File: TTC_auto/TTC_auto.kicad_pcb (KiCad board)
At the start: 2 copper layers, 84.2 x 84.2 mm, 78 parts, among them J1 EPS 3V3, J2 MISSION, J3 SMA edge, J4 SWD TC2030, J5 OBC I2C, J6 OBC UART, J7 EPS 5V, J8 SPARE GPIO, J9 DIPOLE FEED, Q1 AO3401A, U1 TPS7A2033PDBVR, U2 RFM98W-433S2, U3 STM32F446RET6, U4 TMP102, Y1 8MHz, Y2 32.768kHz

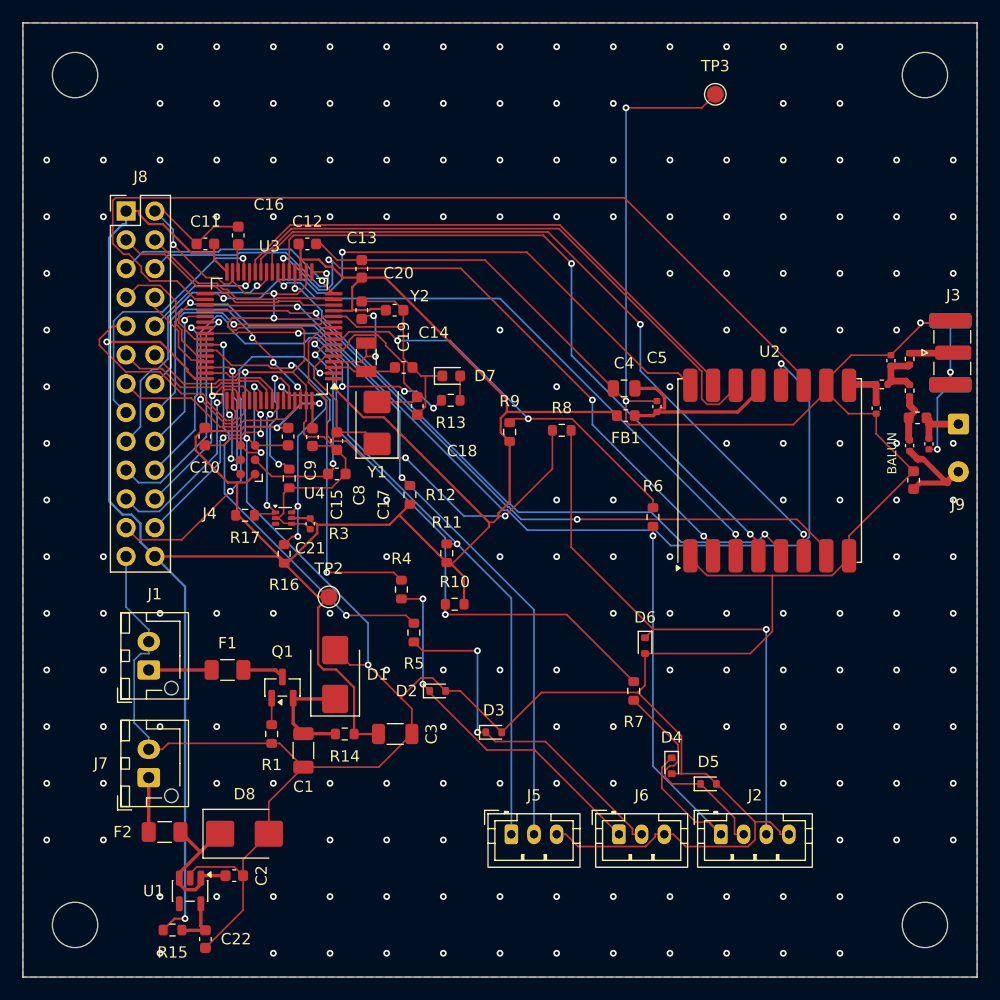
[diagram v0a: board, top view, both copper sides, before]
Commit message: TTC_auto: re-place by functional blocks (structured version)
Parts grouped into Power / MCU / RF / I/O / Sensor regions with
assembly spacing (~0.8 mm, 2 mm round MCU and RF module), crystal pads
matched to MCU pin order, copper keep-out under the RFM98W module,
3 fiducials, per-patch GND vias. Antenna/balun hand-fixed to top layer.
DRC: 0 violations, 0 unconnected, schematic parity clean.
README added.

Co-Authored-By: Claude Opus 5.5 <noreply@anthropic.com>
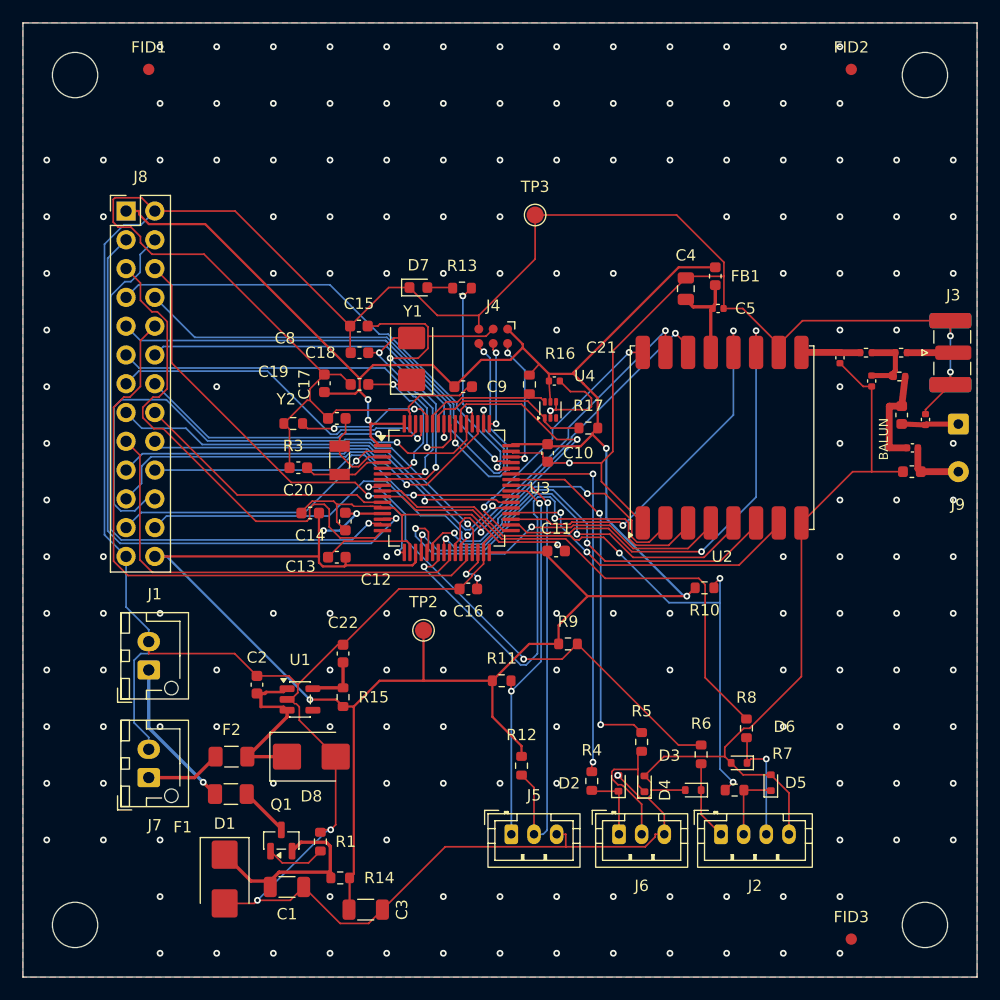
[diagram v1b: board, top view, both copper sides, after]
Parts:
- added FID1: Fiducial, Fiducial_1mm_Mask2mm, F.Cu at (104.0, 97.0)
- added FID2: Fiducial, Fiducial_1mm_Mask2mm, F.Cu at (166.0, 97.0)
- added FID3: Fiducial, Fiducial_1mm_Mask2mm, F.Cu at (166.0, 173.8)
- moved C11 41.1 mm to (139.9, 139.5), turned to 0 degrees
- moved C16 37.2 mm to (132.2, 142.8), turned to 180 degrees
- moved R17 31.3 mm to (142.8, 128.7), turned to 0 degrees
- moved R8 30.9 mm to (156.8, 155.2), turned to 90 degrees
- moved C10 30.3 mm to (139.2, 130.8)
- moved C22 28.0 mm to (121.2, 148.6), turned to 90 degrees
- moved C12 27.8 mm to (120.6, 140.1), turned to 180 degrees
- moved R16 26.3 mm to (137.6, 124.8), turned to -90 degrees
- moved R12 25.9 mm to (136.9, 158.4), turned to 90 degrees
- moved R15 25.5 mm to (121.2, 152.4), turned to -90 degrees
- moved U4 25.4 mm to (139.4, 127.0), turned to 90 degrees
- moved C21 25.0 mm to (139.8, 124.5), turned to 0 degrees
- moved J4 24.2 mm to (134.4, 120.5), turned to 180 degrees
- moved R4 23.8 mm to (143.1, 159.8)
- moved C13 22.3 mm to (121.3, 136.9), turned to -90 degrees
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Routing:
- net /RFM_DIO4: track 80.7 -> 33.4 mm
- net /PB2: track 10.9 -> 55.5 mm, vias 1 -> 0
- net /PD2: track 17.1 -> 58.4 mm, vias 3 -> 1
- net /RFM_DIO3: track 82.6 -> 41.5 mm, vias 0 -> 2
- net Net-(D6-A1): track 49.7 -> 10.7 mm
- net /RFM_DIO5: track 64.3 -> 27.9 mm
- net /PA1: track 18.0 -> 52.5 mm, vias 0 -> 1
- net /PA0: track 20.8 -> 54.4 mm, vias 0 -> 1
- net Net-(D4-A1): track 39.7 -> 6.95 mm, vias 1 -> 0
- net /PC12: track 15.8 -> 48.2 mm
- net /PA11: track 11.7 -> 42.8 mm, vias 0 -> 1
- net /OBC_SCL: track 70.8 -> 39.8 mm, vias 2 -> 1
- net /PA12: track 8.14 -> 38.2 mm, vias 0 -> 1
- net /RFM_RESET: track 64.7 -> 36.4 mm
- net /RFM_DIO2: track 51.9 -> 23.7 mm
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
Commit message: TTC_auto: spread placement for soldering and debugging
Re-placed with larger block areas (MCU and RF use the top strip),
bigger minimum gaps (~1.2 mm small parts, ~3 mm round MCU/radio/debug
pad) and a soft spacing penalty under 2.5 mm, then re-routed with
Freerouting. Median gap to nearest part 0.83 -> 2.03 mm; parts closer
than 1 mm 61 -> 5. Antenna path 36.3 mm, top layer, 0 vias.
DRC: 0 violations, 0 unconnected, schematic parity clean.

Co-Authored-By: Claude Opus 5.5 <noreply@anthropic.com>
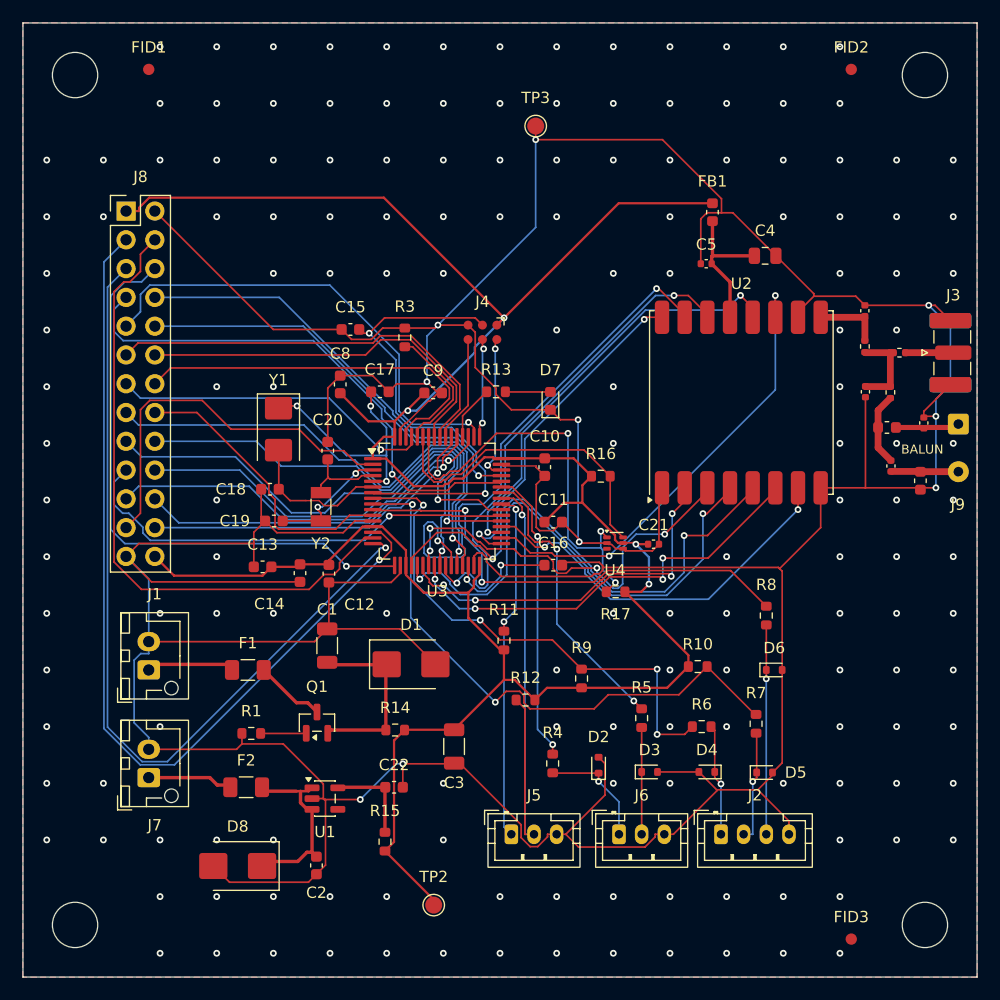
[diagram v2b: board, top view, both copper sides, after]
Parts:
- moved D1 25.1 mm to (127.2, 149.5), turned to 0 degrees
- moved TP2 24.3 mm to (129.2, 170.8), turned to 180 degrees
- moved C1 21.6 mm to (119.8, 147.8), turned to 90 degrees
- moved C21 16.9 mm to (148.6, 138.9)
- moved C2 16.8 mm to (118.8, 167.2), turned to -90 degrees
- moved C3 16.4 mm to (130.9, 156.8), turned to -90 degrees
- moved D7 15.4 mm to (139.4, 126.2), turned to 90 degrees
- moved R17 14.6 mm to (145.2, 143.1)
- moved C18 14.4 mm to (114.7, 134.1)
- moved R14 13.9 mm to (125.8, 155.3)
- moved Y1 13.3 mm to (115.5, 128.8), turned to -90 degrees
- moved R15 13.3 mm to (124.8, 165.2)
- moved U4 13.1 mm to (145.2, 138.8), turned to 0 degrees
- moved C22 12.6 mm to (125.7, 160.3), turned to 0 degrees
- moved R3 12.4 mm to (126.6, 120.7), turned to -90 degrees
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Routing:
- net /PA2: track 44.6 -> 76.0 mm, vias 0 -> 1
- net /PD2: track 58.4 -> 30.6 mm
- net /PA0: track 54.4 -> 81.2 mm
- net /I2C_SCL: track 14.9 -> 36.8 mm, vias 0 -> 3
- net /RFM_DIO1: track 29.1 -> 47.4 mm
- net +3V3: track 253.0 -> 234.7 mm, vias 7 -> 4
- net /PC12: track 48.2 -> 31.7 mm
- net /I2C_SDA: track 11.8 -> 27.9 mm
- net /PA3: track 38.8 -> 51.9 mm, vias 2 -> 1
- net /SPI1_SCK: track 33.5 -> 46.5 mm
- net /PB2: track 55.5 -> 42.9 mm, vias 0 -> 1
- net /RFM_DIO0: track 32.3 -> 44.4 mm
- net /SPI1_MOSI: track 48.1 -> 36.7 mm, vias 2 -> 4
- net /SWO: track 19.9 -> 9.41 mm, vias 2 -> 0
- net /RFM_NSS: track 36.5 -> 46.3 mm
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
